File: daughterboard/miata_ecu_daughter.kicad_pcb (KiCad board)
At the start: 4 copper layers, 125 x 60 mm, 221 parts, among them J1 Mezz_Power_Out, J102 SWD (WBO), J2 Mezz_Signal_In, J3 SWD, Q1 AUIPS2041LTR, Q101 VND14NV04, Q2 AUIPS2041LTR, Q3 AUIPS2041LTR, Q4 AUIPS2041LTR, Q5 AUIPS2041LTR, Q6 AUIPS2041LTR, Q7 AUIPS2041LTR, Q8 AUIPS2041LTR, SW1 BOOT, SW2 RESET, U1 STM32F407VGT6, U10 SN65HVD230DR, U101 MCP6004, U102 STM32F042K6T6, U103 REF3033, U105 AD8628, U106 SN65HVD230DR, U2 LMR14020, U3 TLS115B0EJ, U4 AMS1117-3.3, U5 ULN2003AD, U6 TC4427, U7 TC4427, U8 LMV321IDBVR, U9 MAX9926UAEE+, Y1 8MHz

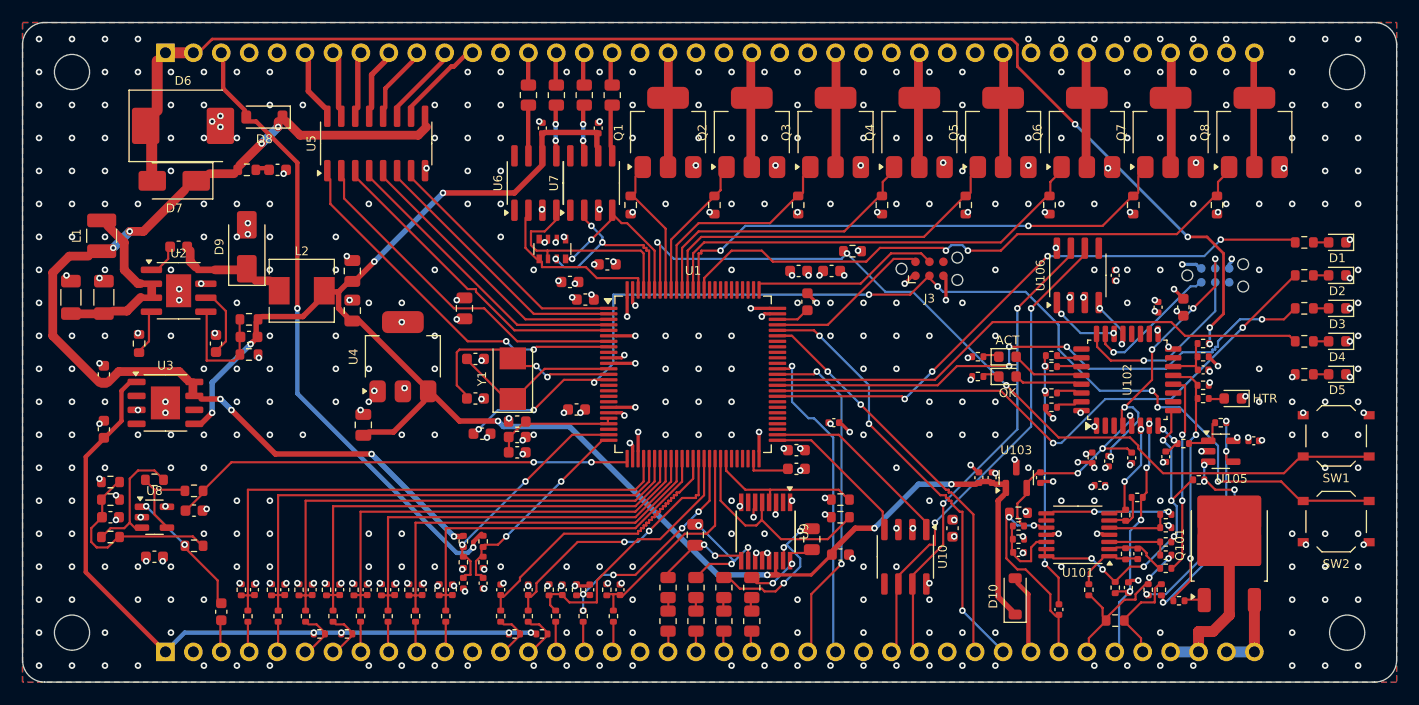
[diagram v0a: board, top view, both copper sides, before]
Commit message: IAT source jumper on every motherboard; wideband MCU flashed through the main MCU
- motherboards (1989-93 / 1994-95 rev 0.5, 1996-97 / 1999-2000 / 2001-05
  rev 0.3): the R4/R5 0R links are replaced by JP1, a 1x3 2.54 mm header with
  a removable shunt (STOCK = harness sensor, EXT = IAT connector, default)
- daughterboard rev 0.4: USART3 (PD8/PD9) to the STM32F042's ROM-bootloader
  USART1 (PA9/PA10), plus PD10 -> its BOOT0 and PD11 -> its NRST, so both
  MCUs can be flashed over the one USB-C port (rusEFI support to be written;
  SWD pads kept as a fallback)
- scripts: schematic check now also catches nets split across sheets;
  motherboard project template bundled
- README: flashing and IAT sections

Co-Authored-By: Claude Opus 5.5 <noreply@anthropic.com>
Claude-Session: https://claude.ai/code/session_012UFcA8PhPqkqYxcgEjD2n9
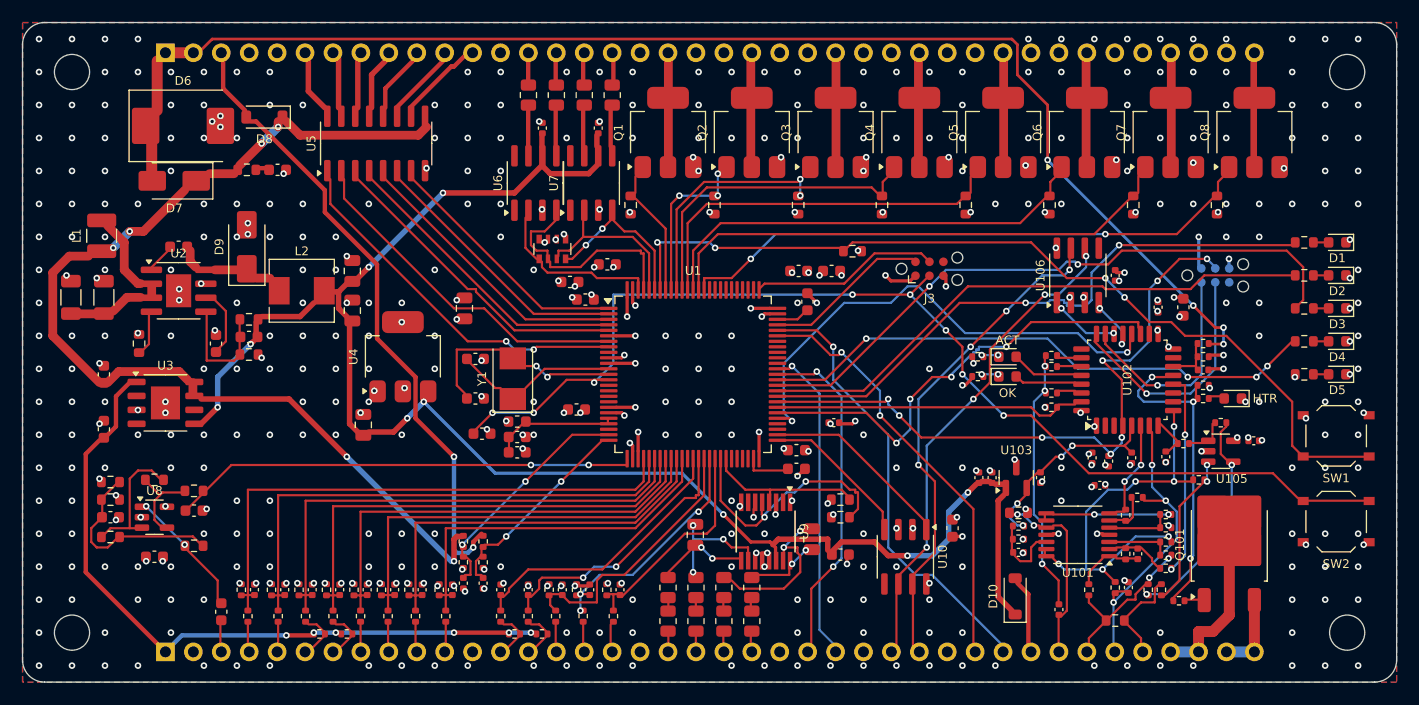
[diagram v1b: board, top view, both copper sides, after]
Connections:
- C116 pad 1: /Wideband controller/WB_NRST -> WB_NRST
- J102 pad 3: /Wideband controller/WB_NRST -> WB_NRST
- R129 pad 2: /Wideband controller/WB_BOOT0 -> WB_BOOT0
- U1 pad 55: (no net) -> WB_PROG_TX
- U1 pad 56: (no net) -> WB_PROG_RX
- U1 pad 57: (no net) -> WB_BOOT0
- U1 pad 58: (no net) -> WB_NRST
- U102 pad 19: (no net) -> WB_PROG_RX
- U102 pad 20: (no net) -> WB_PROG_TX
- U102 pad 31: /Wideband controller/WB_BOOT0 -> WB_BOOT0
- U102 pad 4: /Wideband controller/WB_NRST -> WB_NRST
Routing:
- net WB_NRST: track 0.00 -> 58.3 mm, vias 0 -> 8
- net WB_PROG_TX: track 0.00 -> 45.2 mm, vias 0 -> 2
- net WB_PROG_RX: track 0.00 -> 41.1 mm, vias 0 -> 4
- net WB_BOOT0: track 0.00 -> 27.3 mm
- net /Wideband controller/WB_NRST: track 25.0 -> 0.00 mm, vias 5 -> 0
- net /Wideband controller/WB_VM: track 28.6 -> 36.6 mm
- net /Wideband controller/WB_SWDIO: track 11.6 -> 19.0 mm
- net /Wideband controller/WB_HTR_PWM: track 21.4 -> 28.6 mm, vias 2 -> 3
- net +5V: track 134.0 -> 139.6 mm, vias 8 -> 9
- net /Wideband controller/WB_SWCLK: track 15.9 -> 21.4 mm
- net LSU_VM: track 21.5 -> 26.3 mm, vias 4 -> 3
- net /MCU/LED_WARN: track 52.8 -> 57.4 mm, vias 4 -> 2
- net /Wideband controller/WB_IS_P: track 17.9 -> 13.6 mm, vias 4 -> 2
- net VR2_OUT: track 18.8 -> 22.6 mm, vias 0 -> 2
- net /MCU/LED_COMM: track 54.9 -> 51.3 mm, vias 2 -> 0
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
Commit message: Rev 0.5 daughterboard, rev 0.6 1989-93/1994-95 motherboards: review fixes
Daughterboard rev 0.5:
- SN74LVC4245A drives the eight AUIPS2041 low sides at 5 V; output enable pulled
  off (R71) until the firmware enables it on PA8.
- BOOT1 pull-down (R72); hall input clamps D13/D14.
- ULN2003 COM to an SMAJ33A TVS (D11) instead of +12V: no key-off back-feed,
  no conduction in a 35 V load dump.
- Logic supply: D7/D8 -> 0.5 A PTC F1 -> SMAJ33A D12; C16 50 V, SS36 D9, C59.
- Tach stays an output.

Motherboards:
- Idle/VVT freewheel diodes, 4.7k switch pull-up options (not fitted),
  AUX VBAT PTC on all years.
- 1989-93 rev 0.6: two drivers per injector wire (0R links), SMCJ40A clamps.
- 2001-05: J1 3B tied to 3A.

Firmware: low-side enable (inverted open drain, forced writes, off during
configuration changes), unused control pins parked with pull-down, 1989-93
batch on all four outputs, VBATT offset noted.

Verification: 18/18 board tests, 119/119 harness check, circuit sims
20 OK / 3 CHECK / 6 REF / 0 FAIL, flash sim 9/9, firmware and bootloader
build; all boards 0 unconnected, 0 clearance errors.

Co-Authored-By: Claude Opus 5.5 <noreply@anthropic.com>
Claude-Session: https://claude.ai/code/session_012UFcA8PhPqkqYxcgEjD2n9
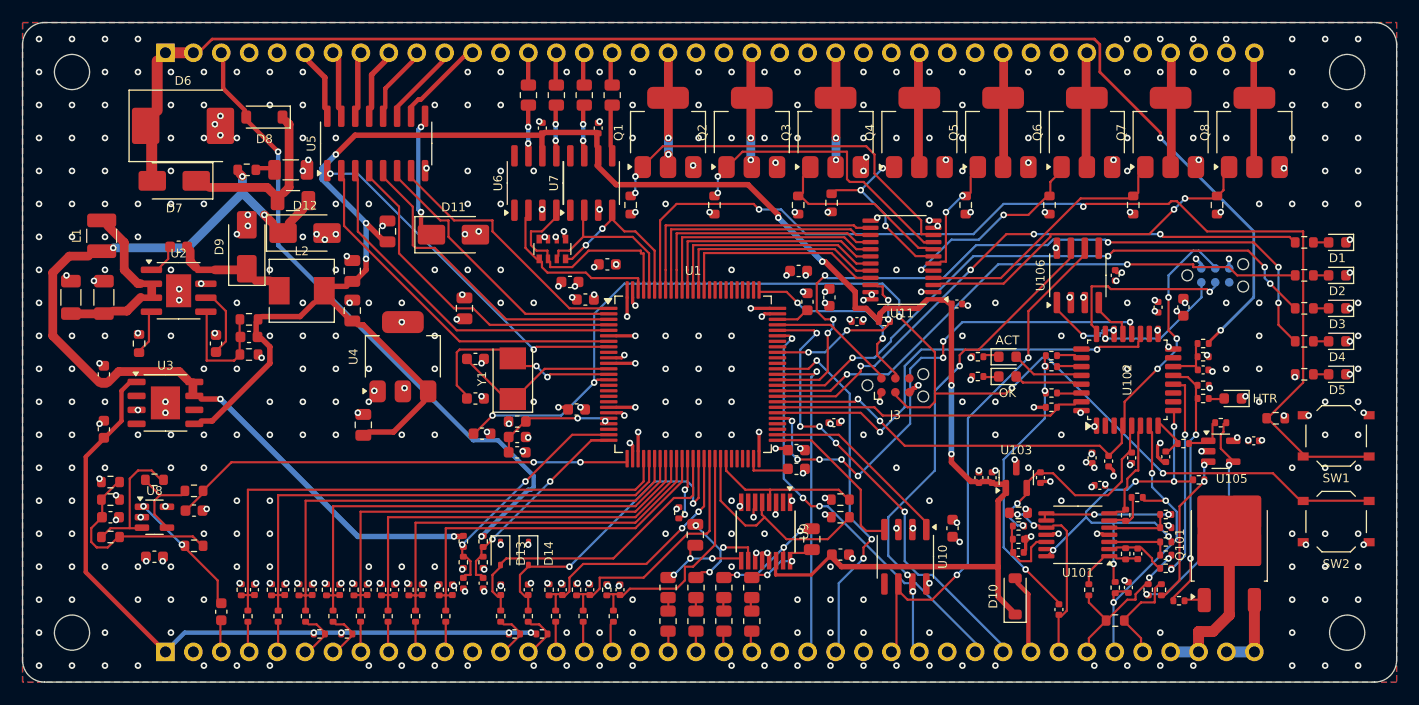
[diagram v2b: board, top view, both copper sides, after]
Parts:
- added C57: 100n, Capacitor_SMD:C_0402_1005Metric, F.Cu at (185.0, 75.6)
- added C58: 100n, Capacitor_SMD:C_0402_1005Metric, F.Cu at (175.9, 77.2)
- added C59: 10u, Capacitor_SMD:C_0805_2012Metric, F.Cu at (133.2, 69.0)
- added D11: SMAJ33A, Diode_SMD:D_SMA, F.Cu at (139.2, 69.3)
- added D12: SMAJ33A, Diode_SMD:D_SMA, F.Cu at (125.7, 69.2)
- added D13: 1N4148WS, Diode_SMD:D_SOD-323, F.Cu at (143.5, 98.3)
- added D14: 1N4148WS, Diode_SMD:D_SOD-323, F.Cu at (146.0, 98.3)
- added F1: SMD1206P050TF/24, Fuse:Fuse_1206_3216Metric, F.Cu at (124.6, 66.2)
- added R71: 10k, Resistor_SMD:R_0402_1005Metric, F.Cu at (178.4, 77.2)
- added R72: 10k, Resistor_SMD:R_0402_1005Metric, F.Cu at (159.7, 94.6)
- added U11: SN74LVC4245APWR, Package_SO:TSSOP-24_4.4x7.8mm_P0.65mm, F.Cu at (180.0, 71.6)
- C16: value 4.7u -> 10u/50V; footprint Capacitor_SMD:C_0603_1608Metric -> Capacitor_SMD:C_1206_3216Metric
- D9: value SS34 -> SS36
- moved R1 41.4 mm to (214.0, 86.0)
- moved J3 11.0 mm to (179.4, 83.0)
- moved R22 4.58 mm to (173.6, 66.4)
- moved C7 2.41 mm to (173.4, 75.0), turned to 90 degrees
- moved C16 1.20 mm to (124.4, 63.4)
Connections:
- D7 pad 1: +12V -> /Power/+12V_IN
- D8 pad 1: +12V -> /Power/+12V_IN
- Q1 pad 1: INJ1_CTL -> /Outputs/INJ1_IN
- Q2 pad 1: INJ2_CTL -> /Outputs/INJ2_IN
- Q3 pad 1: INJ3_CTL -> /Outputs/INJ3_IN
- Q4 pad 1: INJ4_CTL -> /Outputs/INJ4_IN
- Q5 pad 1: IACV_CTL -> /Outputs/IACV_IN
- Q6 pad 1: VVT_CTL -> /Outputs/VVT_IN
- Q7 pad 1: BOOST_CTL -> /Outputs/BOOST_IN
- Q8 pad 1: ALT_CTL -> /Outputs/ALT_IN
- R19 pad 1: INJ1_CTL -> /Outputs/INJ1_IN
- R20 pad 1: INJ2_CTL -> /Outputs/INJ2_IN
- R21 pad 1: INJ3_CTL -> /Outputs/INJ3_IN
- R22 pad 1: INJ4_CTL -> /Outputs/INJ4_IN
- R23 pad 1: IACV_CTL -> /Outputs/IACV_IN
- R24 pad 1: VVT_CTL -> /Outputs/VVT_IN
- R25 pad 1: BOOST_CTL -> /Outputs/BOOST_IN
- R26 pad 1: ALT_CTL -> /Outputs/ALT_IN
- U1 pad 37: (no net) -> /MCU/BOOT1
- U1 pad 67: (no net) -> DRV_EN_N
- U5 pad 9: +12V -> /Outputs/ULN_COM
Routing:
- net ALT_CTL: track 52.5 -> 19.4 mm, vias 2 -> 0
- net /Outputs/INJ1_IN: track 0.00 -> 32.3 mm, vias 0 -> 2
- net /Outputs/ALT_IN: track 0.00 -> 29.7 mm, vias 0 -> 2
- net +5V: track 139.6 -> 165.7 mm, vias 9 -> 7
- net BOOST_CTL: track 46.1 -> 20.1 mm
- net /Outputs/INJ2_IN: track 0.00 -> 24.5 mm, vias 0 -> 2
- net /Outputs/BOOST_IN: track 0.00 -> 21.8 mm
- net VVT_CTL: track 39.2 -> 20.8 mm
- net /MCU/BOOT0: track 78.1 -> 96.3 mm, vias 4 -> 2
- net /Outputs/VVT_IN: track 0.00 -> 16.1 mm, vias 0 -> 2
- net /MCU/LED_ERR: track 51.1 -> 66.0 mm, vias 4 -> 6
- net DRV_EN_N: track 0.00 -> 14.7 mm, vias 0 -> 4
- net /Outputs/INJ4_IN: track 0.00 -> 14.6 mm, vias 0 -> 3
- net /Outputs/INJ3_IN: track 0.00 -> 14.6 mm
- net INJ1_CTL: track 10.9 -> 24.5 mm
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
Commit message: Daughterboard: 5.5 A buck inductor, 33 pF crystal caps; NB alternator control off by default
- L2: Sunlord MWSA0603S-100MT (C132141, 10 uH, Isat 5.5 A, 7 x 6.6 mm). The
  MWSA0503S saturated at 3.5 A, below the LMR14020's 3.8 A maximum current
  limit. Placed on end; D9 and the feedback divider moved 0.3 mm left.
- C13/C14: 33 pF C0G (C1663) for the 20 pF crystal (were 22 pF).
- Firmware: NB alternator control ships off until the field current is
  measured (pin, PID and target still set up). Test checks the field isn't
  driven with the default tune.
- Daughterboard re-routed and released: 754 pads match, 0 unconnected,
  0 clearance errors. Viewer assets and README renders refreshed.

Co-Authored-By: Claude Opus 5.5 <noreply@anthropic.com>
Claude-Session: https://claude.ai/code/session_012UFcA8PhPqkqYxcgEjD2n9
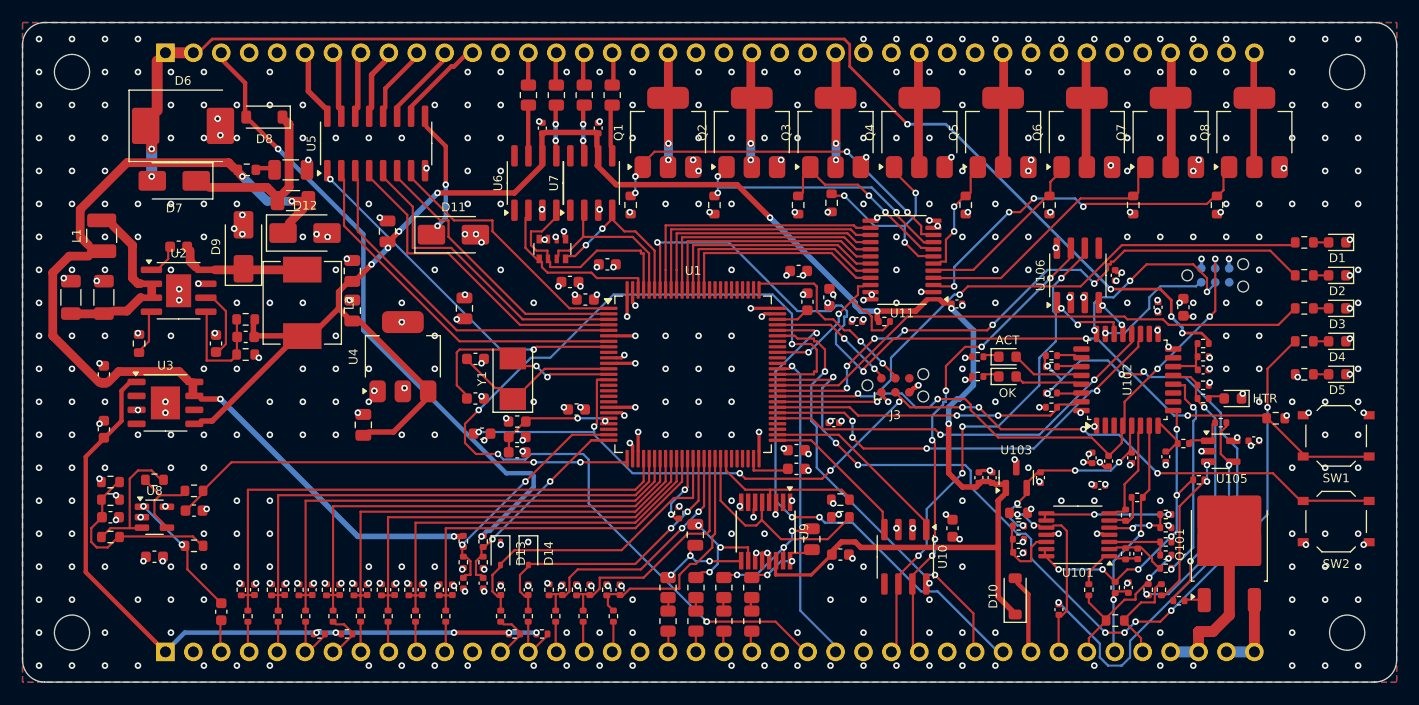
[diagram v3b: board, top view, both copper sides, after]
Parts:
- C13, C14: value 22p -> 33p
- L2: footprint Inductor_SMD:L_Sunlord_MWSA0503S -> Inductor_SMD:L_Sunlord_MWSA0603S
- moved L2 1.10 mm to (125.5, 75.5), turned to -90 degrees
- moved D9 0.30 mm to (120.1, 70.4)
- moved C21 0.30 mm to (120.3, 78.6)
- moved R10 0.30 mm to (120.3, 80.2)
- moved R9 0.30 mm to (120.3, 77.0)
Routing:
- net UART_TX: track 28.6 -> 89.0 mm, vias 1 -> 4
- net /Wideband controller/WB_ESR: track 25.6 -> 58.3 mm, vias 3 -> 5
- net /MCU/LED_ERR: track 66.0 -> 81.2 mm, vias 6 -> 8
- net /MCU/BOOT0: track 96.3 -> 81.7 mm, vias 2 -> 4
- net /MCU/NRST: track 109.6 -> 95.4 mm, vias 5 -> 9
- net +5V: track 165.7 -> 153.5 mm, vias 7 -> 8
- net VBAT_IN: track 124.8 -> 114.4 mm, vias 2 -> 6
- net WB_PROG_TX: track 46.5 -> 36.4 mm, vias 8 -> 2
- net /Wideband controller/WB_VM: track 36.2 -> 27.5 mm
- net +12V: track 74.9 -> 81.6 mm, vias 5 -> 4
- net LSU_VM: track 26.3 -> 21.5 mm, vias 3 -> 2
- net /MCU/LED_WARN: track 54.6 -> 50.2 mm, vias 4 -> 0
- net USB_DP: track 41.8 -> 46.1 mm, vias 5 -> 3
- net UART_RX: track 32.9 -> 28.7 mm, vias 3 -> 1
- net /MCU/LED_COMM: track 52.1 -> 55.5 mm, vias 2 -> 6
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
